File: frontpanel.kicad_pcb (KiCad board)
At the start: 2 copper layers, 172.5 x 128.3 mm, 105 parts, among them J601 PJ301CM, J602 PJ301CM, J603 PJ301BM, J604 PJ301BM, J605 PJ301BM, J606 PJ301BM, J607 PJ301BM, J608 PJ301BM, J609 PJ301BM, J610 PJ301BM, J611 PJ301BM, J612 PJ301BM, J613 PJ301BM, J614 PJ301BM, J615 PJ301BM, J616 PJ301BM, J617 PJ301BM, J618 PJ301BM, J619 PJ301BM, J620 PJ301BM, J621 PJ301BM, J622 PJ301BM, J623 PJ301BM, J624 PJ301BM, J625 PJ301BM, J626 PJ301BM, SW301 TL1105T, SW302 TL1105T, SW303 TL1105T, SW304 TL1105T, SW305 TL1105T, SW317 TL1105T, SW318 TL1105T, SW319 TL1105T, SW320 TL1105T, SW321 TL1105T, SW322 TL1105T, SW323 TL1105T, SW324 TL1105T, SW325 TL1105T, SW326 TL1105T, SW327 TL1105T, SW328 TL1105T, SW329 TL1105T, SW330 TL1105T, SW331 TL1105T, SW332 TL1105T, SW333 TL1105T, SW334 TL1105T, SW335 TL1105T, SW336 TL1105T, SW337 TL1105T, SW338 TL1105T, SW339 TL1105T, SW340 TL1105T

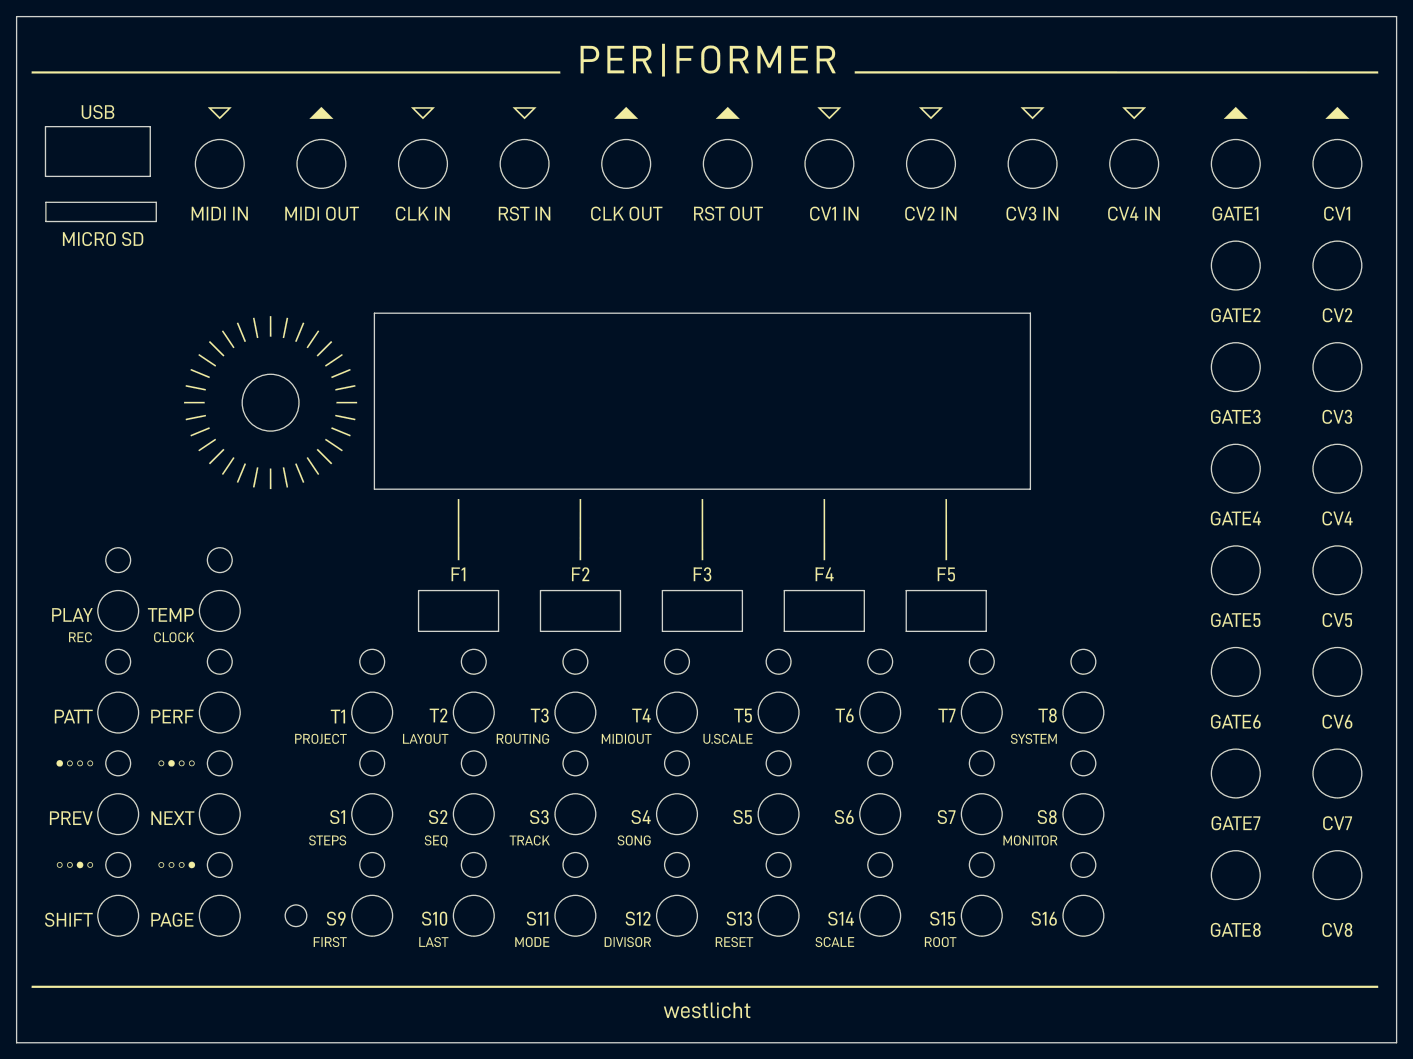
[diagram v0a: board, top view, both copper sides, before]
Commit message: Some cleanup. Frontpanel with Copper Labels.
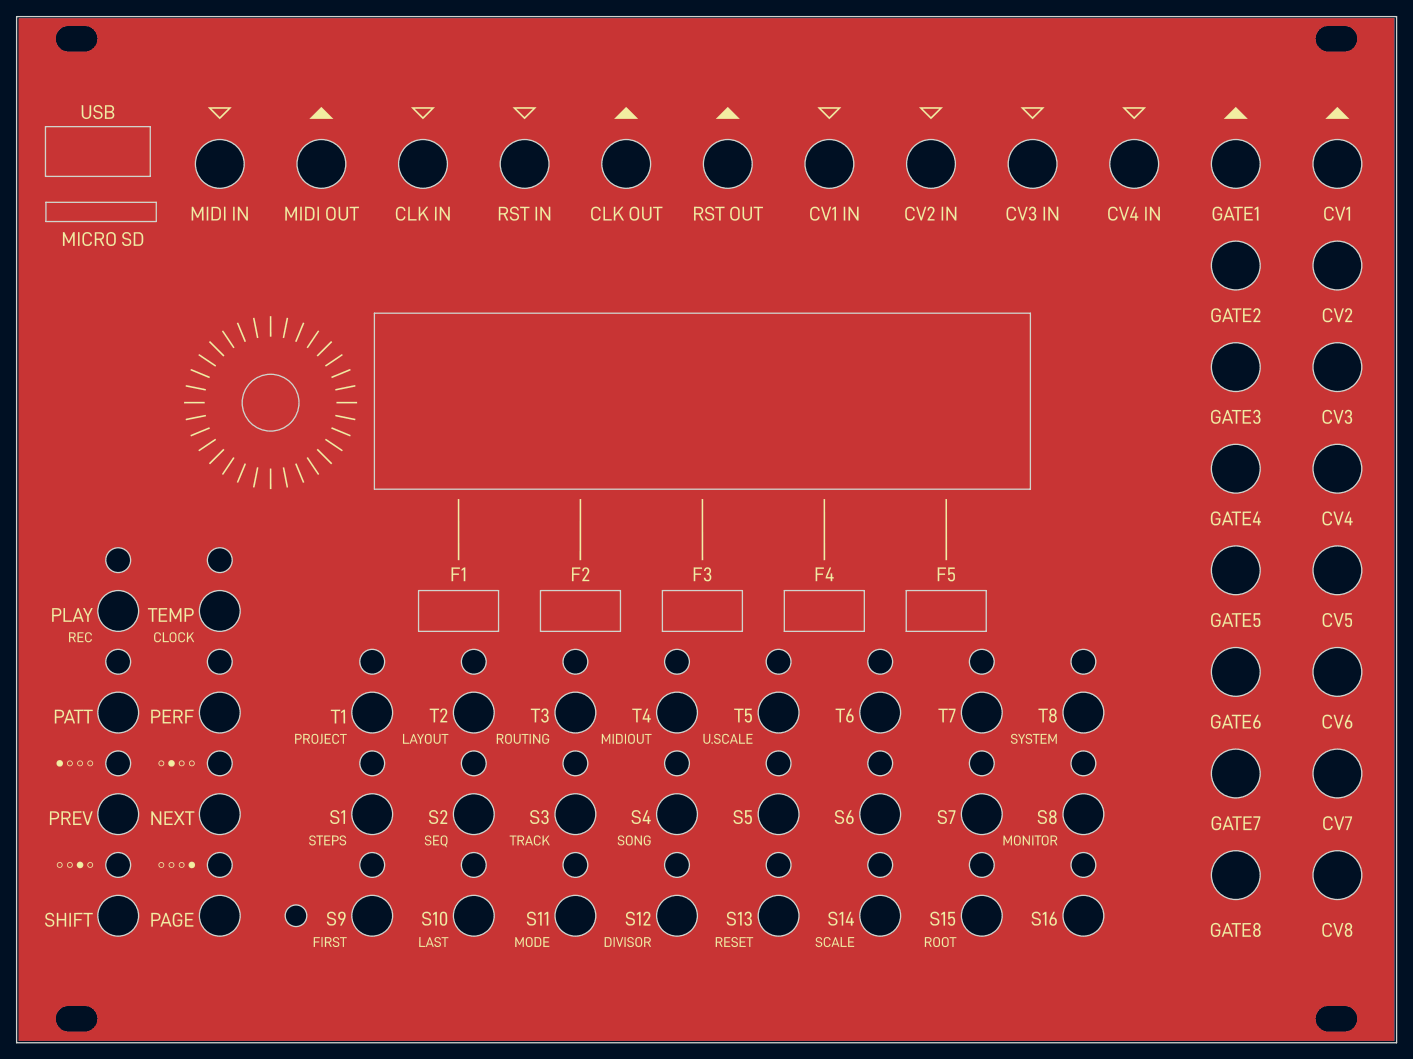
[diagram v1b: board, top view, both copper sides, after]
